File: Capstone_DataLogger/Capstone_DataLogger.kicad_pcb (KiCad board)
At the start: 2 copper layers, 70 x 130 mm, 26 parts, among them J1 S2B-PH-K-SLFSN, J10 RJ9, J3 S5B-PH-K-S, J7 S4B-PH-K-SLFSN, J8 S4B-PH-K-SLFSN, J9 S4B-PH-K-SLFSN, Q1 NMOS, U2 ESP32-DEVKITC-32D, U3 ATmega328-P, U4 MCP7940M-I/P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

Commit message: Revised PCB
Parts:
- removed C1, C3, C5: 100n, Capacitor_SMD:C_1206_3216Metric_Pad1.33x1.80mm_HandSolder
- removed C4: 100p, Capacitor_SMD:C_1206_3216Metric_Pad1.33x1.80mm_HandSolder
- removed D2, D3: LED, Diode_SMD:D_1206_3216Metric_Pad1.42x1.75mm_HandSolder
- removed Q1: NMOS, Package_TO_SOT_THT:TO-220-3_Horizontal_TabDown
- removed R6: 1k, Resistor_SMD:R_1206_3216Metric_Pad1.30x1.75mm_HandSolder
- removed U5: TLV172IDCK, Package_TO_SOT_SMD:SOT-353_SC-70-5
- removed U7: SN74HC08N, Capstone:N14
- added J2: S2B-PH-K-SLFSN, Capstone:CONN_S2B-PH-K-S_JST, F.Cu at (135.1, 109.0)
- added J4: S2B-PH-K-SLFSN, Capstone:CONN_S2B-PH-K-S_JST, F.Cu at (135.1, 121.0)
- added J5: S2B-PH-K-SLFSN, Capstone:CONN_S2B-PH-K-S_JST, F.Cu at (145.1, 121.0)
- added XTAL1: PS1240P02BT, Capstone:XTAL_PS1240P02BT_TDK, F.Cu at (118.0, 110.0)
- R1: value 10k -> 1k
- moved U1 79.1 mm to (158.3, 41.7)
- moved C2 63.1 mm to (165.0, 82.4), turned to 90 degrees
- moved R2 51.0 mm to (169.0, 66.0), turned to -90 degrees
- moved R5 41.3 mm to (137.0, 103.8), turned to -90 degrees
- moved Y2 30.9 mm to (150.5, 103.5), turned to 90 degrees
- moved U4 24.2 mm to (154.1, 102.4)
- moved J1 22.2 mm to (145.1, 109.0)
- moved J9 21.7 mm to (135.1, 135.0), turned to 0 degrees
- moved J7 20.7 mm to (149.1, 135.0), turned to 0 degrees
- moved R1 19.9 mm to (132.2, 103.8), turned to -90 degrees
- moved R3 19.4 mm to (166.0, 66.0), turned to 90 degrees
- moved U2 18.8 mm to (137.3, 71.9)
- moved J10 18.1 mm to (120.9, 124.7)
- moved U3 15.2 mm to (154.1, 64.6)
- moved J8 6.49 mm to (163.1, 135.0), turned to 0 degrees
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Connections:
- J1 pad 1: Net-(U3-PD5) -> Net-(J1-Pad1)
- J1 pad 2: GND -> Net-(J1-Pad2)
- J10 pad 1: +5V_CTRL -> +5V
- J3 pad 3: Net-(U5-+) -> /MCU/VBAT
- J7 pad 1: +5V_CTRL -> +5V
- J8 pad 1: +5V_CTRL -> +5V
- J9 pad 1: +5V_CTRL -> +5V
- R1 pad 1: +5V -> /MCU/WIFI_STAT
- R1 pad 2: /MCU/MFP -> Net-(J1-Pad1)
- R5 pad 1: /MCU/ON_LED -> +5V
- U1 pad 1: +5V -> +3.3V
- U1 pad 2: Net-(U1-D0) -> GND
- U1 pad 3: Net-(U1-D1) -> /MCU/D0
- U1 pad 4: Net-(U1-D2) -> /MCU/CMD
- U1 pad 5: Net-(U1-D3) -> /MCU/CLK
- U1 pad 6: Net-(U1-CMD) -> /MCU/D3
- U1 pad 7: Net-(U1-CLK) -> /MCU/D2
- U1 pad 8: GND -> /MCU/D1
- U1 pad 9: unconnected-(U1-Pad9) -> /MCU/CD
- U2 pad J2-12: Net-(U1-CLK) -> /MCU/CLK
- U2 pad J2-13: Net-(U1-D2) -> /MCU/D2
- U2 pad J2-15: Net-(U1-D3) -> /MCU/D3
- U2 pad J3-13: Net-(U1-D1) -> /MCU/D1
- U2 pad J3-15: Net-(U1-D0) -> /MCU/D0
- U2 pad J3-16: Net-(U1-CMD) -> /MCU/CMD
- U3 pad 11: Net-(U3-PD5) -> unconnected-(U3-PD5-Pad11)
- U3 pad 14: /MCU/MFP -> unconnected-(U3-PB0-Pad14)
- U3 pad 23: /MCU/VBAT -> /MCU/THERM
- U3 pad 24: /MCU/THERM -> /MCU/WIFI_STAT
- U3 pad 25: unconnected-(U3-PC2-Pad25) -> /MCU/VBAT
- U3 pad 4: /MCU/5V_CTRL -> unconnected-(U3-PD2-Pad4)
- U4 pad 7: /MCU/MFP -> unconnected-(U4-MFP-Pad7)
- Y2 pad 1: Net-(U4-X2) -> Net-(U4-X1)
- Y2 pad 2: Net-(U4-X1) -> Net-(U4-X2)
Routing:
- net GND: track 317.0 -> 3.69 mm
- net +5V: track 251.0 -> 0.00 mm, vias 0 -> 1
- net +5V_CTRL: track 153.8 -> 0.00 mm, vias 1 -> 0
- net +3.3V: track 102.4 -> 0.00 mm
- net Net-(D3-A): track 75.1 -> 0.00 mm
- net /MCU/BUZZER: track 0.00 -> 70.2 mm
- net Net-(J4-Pad1): track 62.7 -> 0.00 mm
- net /MCU/PWM_HEATER: track 38.2 -> 99.1 mm
- net /MCU/D3: track 0.00 -> 55.9 mm
- net /MCU/IND_1: track 52.0 -> 0.00 mm
- net /MCU/D0: track 0.00 -> 49.3 mm
- net Net-(U1-CLK): track 48.8 -> 0.00 mm
- net /MCU/ESP_EN: track 47.8 -> 0.00 mm
- net /MCU/CMD: track 0.00 -> 47.6 mm
- net /MCU/CLK: track 0.00 -> 46.3 mm
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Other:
- board text added: "+3V3_IN"
- board text added: "+5V"
- board text added: "+5V_IN"
- board text added: "ATMEGA328P"
- board text added: "ESP32"
- board text added: "GND"
- board text added: "M1 or M2 holes in the corners"
- board text added: "PWM_HEATER"
- board text added: "PWR CONN"
- board text added: "PWR. LED"
- board text added: "RS_1"
- board text added: "RS_2"
- board text added: "RTC"
- board text added: "SCL"
- board text added: "SDA"
- board text added: "SENSOR_1"
- board text added: "SENSOR_2"
- board text added: "SENSOR_3"
- board text added: "VBAT"
- board text added: "WIFI_LED"

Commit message: Last revision before oreder
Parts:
- added J11: Conn_01x04_Socket, Connector_PinSocket_2.54mm:PinSocket_1x04_P2.54mm_Horizontal, F.Cu at (137.5, 109.4)
- added J12: S2B-PH-K-SLFSN, Capstone:CONN_B2B-XH-A_JST, F.Cu at (165.5, 94.5)
- added J6: Conn_01x08_Pin, Connector_PinHeader_2.54mm:PinHeader_1x08_P2.54mm_Vertical, F.Cu at (152.0, 67.3)
- added R4: 10k, Resistor_SMD:R_1206_3216Metric_Pad1.30x1.75mm_HandSolder, F.Cu at (151.0, 59.5)
- added R7: 10k, Resistor_SMD:R_1206_3216Metric_Pad1.30x1.75mm_HandSolder, F.Cu at (151.0, 62.5)
- J1, J2, J4, J5: footprint Capstone:CONN_S2B-PH-K-S_JST -> Capstone:CONN_B2B-XH-A_JST
- J10: footprint Connector_RJ:RJ9_Evercom_5301-440xxx_Horizontal -> Capstone:RJ9
- J3: footprint Capstone:CONN_S5B-PH-K-S_JST -> Capstone:CONN_B5B-XH-A_JST
- J7, J8, J9: footprint Capstone:CONN_S4B-PH-K-S_JST -> Capstone:CONN_B4B-XH-A_JST
- moved XTAL1 75.4 mm to (153.5, 43.5)
- moved J3 56.7 mm to (167.5, 68.5)
- moved R1 53.6 mm to (151.0, 53.5), turned to 180 degrees
- moved R5 49.3 mm to (151.0, 56.5), turned to 180 degrees
- moved J8 31.3 mm to (165.5, 103.8), turned to 90 degrees
- moved J9 30.6 mm to (165.5, 131.8), turned to 90 degrees
- moved C2 30.0 mm to (157.1, 53.5), turned to 0 degrees
- moved J5 29.3 mm to (118.0, 132.0), turned to 90 degrees
- moved J10 29.1 mm to (149.4, 118.6)
- moved J1 28.9 mm to (127.5, 131.9), turned to 90 degrees
- moved J4 28.8 mm to (108.5, 132.0), turned to 90 degrees
- moved U3 26.2 mm to (137.0, 44.8)
- moved J7 23.8 mm to (165.5, 117.8), turned to 90 degrees
- moved J2 22.9 mm to (137.0, 131.8), turned to 90 degrees
- moved U2 18.2 mm to (119.3, 68.8)
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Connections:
- U3 pad 1: unconnected-(U3-~{RESET}/PC6-Pad1) -> /MCU/~{RESET}
- U3 pad 17: unconnected-(U3-PB3-Pad17) -> /MCU/MOSI
- U3 pad 18: unconnected-(U3-PB4-Pad18) -> /MCU/MISO
- U3 pad 19: unconnected-(U3-PB5-Pad19) -> /MCU/SCK
- U3 pad 26: unconnected-(U3-PC3-Pad26) -> /MCU/VIBE_SENSE
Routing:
- net /MCU/SDA: track 145.6 -> 0.00 mm
- net /MCU/SCL: track 139.2 -> 0.00 mm
- net /MCU/PWM_HEATER: track 99.1 -> 0.00 mm
- net /MCU/BUZZER: track 70.2 -> 0.00 mm
- net /MCU/D3: track 55.9 -> 0.00 mm
- net /MCU/VBAT: track 50.1 -> 0.00 mm
- net /MCU/D0: track 49.3 -> 0.00 mm
- net /MCU/CMD: track 47.6 -> 0.00 mm
- net /MCU/CLK: track 46.3 -> 0.00 mm
- net /MCU/D2: track 45.7 -> 0.00 mm
- net /MCU/D1: track 30.4 -> 0.00 mm
- net /MCU/ESP_TX: track 18.7 -> 0.00 mm
- net /MCU/ESP_RX: track 14.6 -> 0.00 mm
- net Net-(U4-X1): track 3.73 -> 0.00 mm
- net Net-(U4-X2): track 3.73 -> 0.00 mm
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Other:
- board text added: "ECE 490/1 CAPSTONE SSULPEP DATA LOGGER BRIDGE BASIC SOLUTIONS"
- board text added: "HEATER"
- board text added: "MAX SCHATZ STEVEN SAGER"
- board text added: "PICKIT CONN"
- board text added: "P_SENSE"
- board text added: "SD CARD"
- board text added: "TEJAS RAVISH DAMIAN HUSKIC"
- board text added: "THERM"
- board text removed: "M1 or M2 holes in the corners"
- board text removed: "PWM_HEATER"

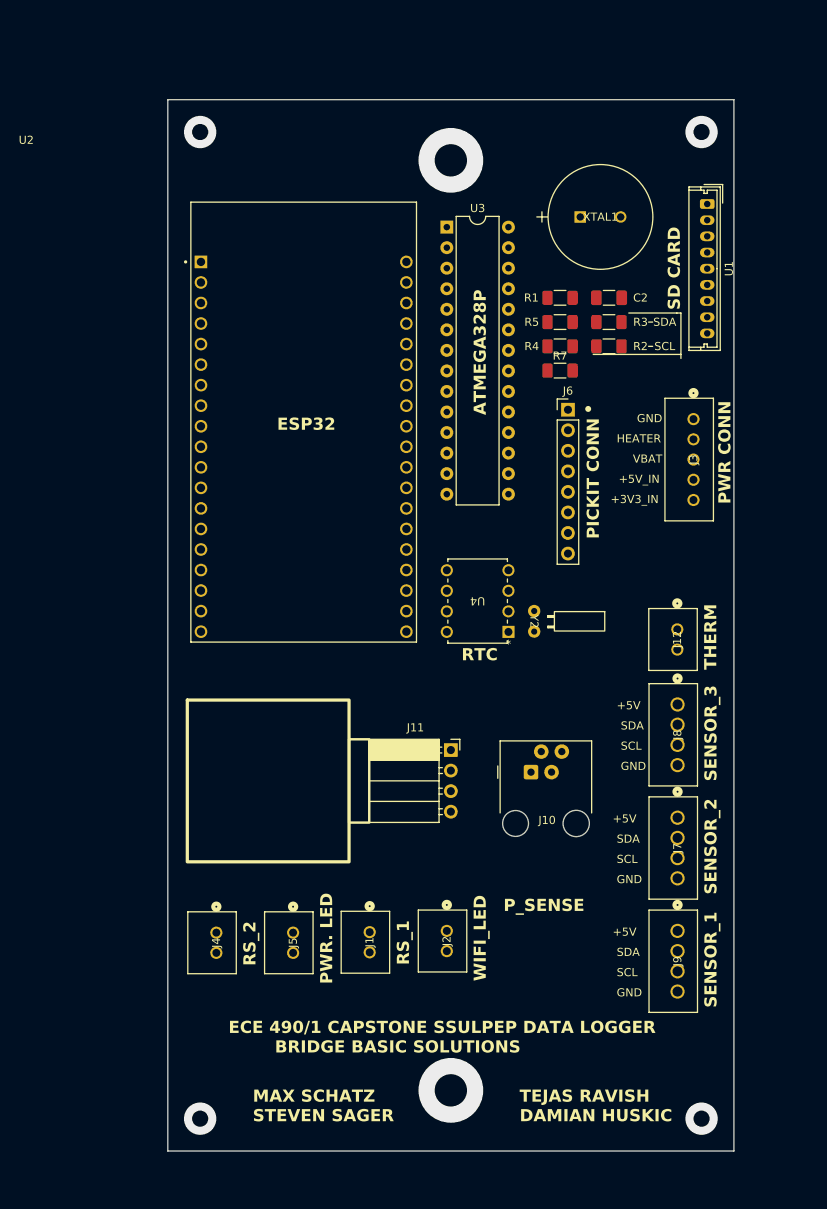
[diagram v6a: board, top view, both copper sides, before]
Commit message: NVM another revision before order, should be good now
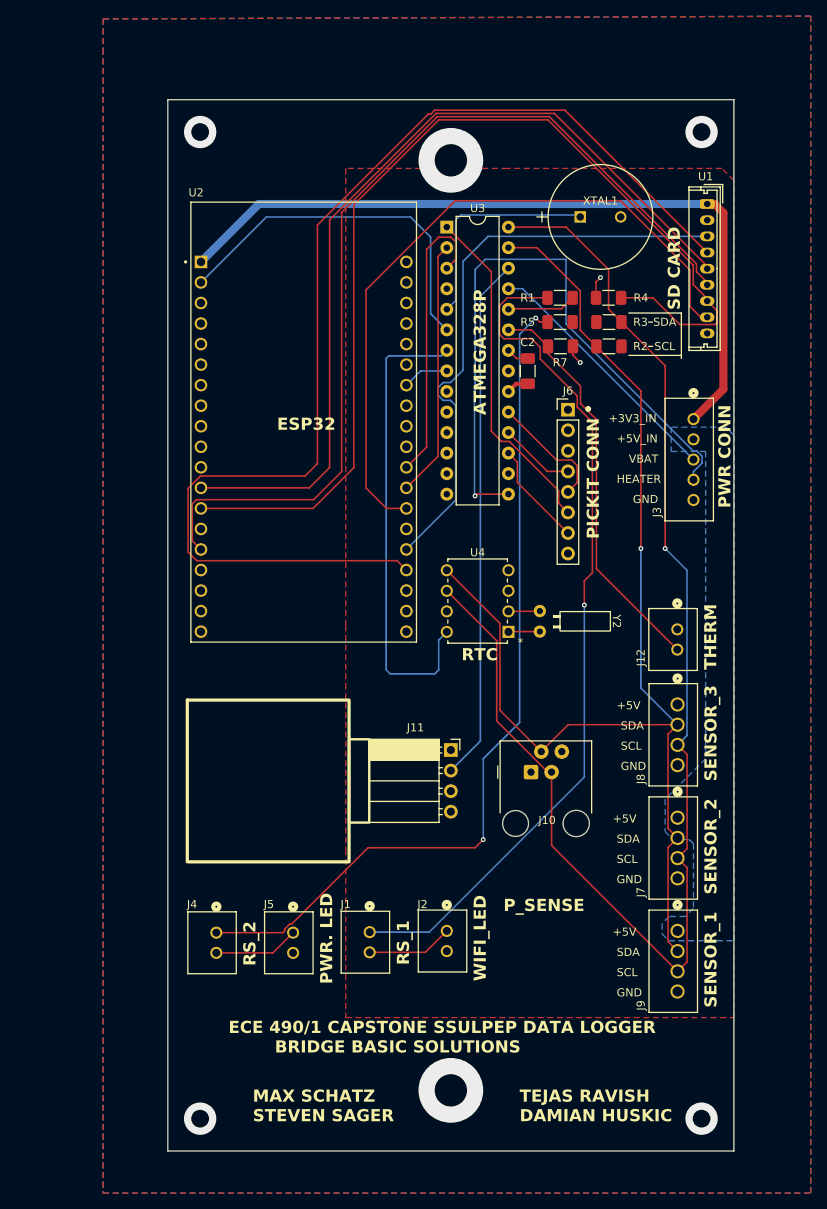
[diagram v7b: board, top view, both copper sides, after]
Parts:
- moved C2 13.5 mm to (147.0, 62.6), turned to 90 degrees
- moved R4 8.49 mm to (157.0, 53.5)
- moved R7 3.00 mm to (151.1, 59.5)
- moved Y2 0.70 mm to (148.5, 93.5)
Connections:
- U3 pad 12: /MCU/IND_1 -> unconnected-(U3-PD6-Pad12)
- U3 pad 13: /MCU/ON_LED -> unconnected-(U3-PD7-Pad13)
- U3 pad 15: unconnected-(U3-PB1-Pad15) -> /MCU/PWM_HEATER
- U3 pad 9: /MCU/PWM_HEATER -> unconnected-(U3-XTAL1/PB6-Pad9)
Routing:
- net /MCU/SCL: track 0.00 -> 166.9 mm, vias 0 -> 1
- net /MCU/SDA: track 0.00 -> 145.2 mm, vias 0 -> 1
- net /MCU/CMD: track 0.00 -> 143.9 mm
- net /MCU/D2: track 0.00 -> 128.9 mm
- net /MCU/D3: track 0.00 -> 117.7 mm
- net /MCU/CLK: track 0.00 -> 107.9 mm
- net Net-(J4-Pad1): track 0.62 -> 107.4 mm, vias 0 -> 2
- net Net-(J1-Pad1): track 0.00 -> 106.3 mm, vias 0 -> 1
- net +3.3V: track 0.00 -> 95.1 mm
- net /MCU/D1: track 0.00 -> 85.9 mm
- net /MCU/PWM_HEATER: track 0.00 -> 79.0 mm, vias 0 -> 1
- net /MCU/D0: track 0.00 -> 72.9 mm
- net /MCU/VIBE_SENSE: track 0.00 -> 65.1 mm
- net +5V: track 0.00 -> 61.2 mm
- net /MCU/THERM: track 0.00 -> 49.9 mm
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- added copper zone on B.Cu, net +5V
- added copper zone on F.Cu, net +5V
- added copper zone on B.Cu, net GND
- added copper zone on F.Cu, net GND
